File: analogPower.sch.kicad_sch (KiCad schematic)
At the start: 27 parts, among them J1 6120XX21621_61201021621, Q1 MMBT3904, Q2 MMBT3904, U10 TL072, U2 REF02CS, U3 TL072, U8 TL072

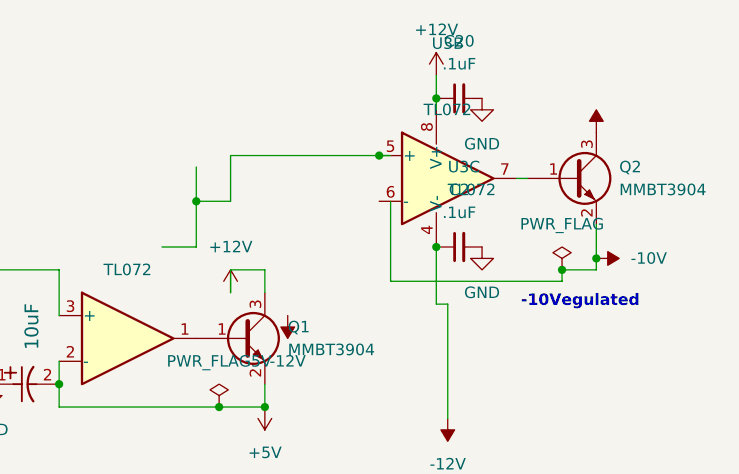
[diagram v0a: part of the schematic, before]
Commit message: added power schematic
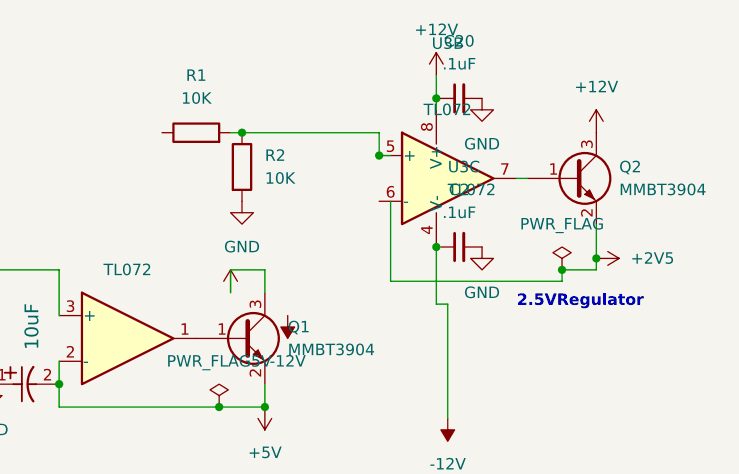
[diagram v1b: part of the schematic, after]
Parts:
- added R1: 10K, Resistor_SMD:R_0603_1608Metric_Pad0.98x0.95mm_HandSolder, symbol Device:R
- added R2: 10K, symbol Device:R
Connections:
- net +12V: now also Q2.3 (C)
- net -12V: no longer Q2.3 (C)
- net GND: now also R2.2
- net at U3.5 (+): now also R1.2, R2.1
- net -10V renamed +2V5
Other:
- note added: "2.5VRegulator"
- note removed: "-10Vegulated"

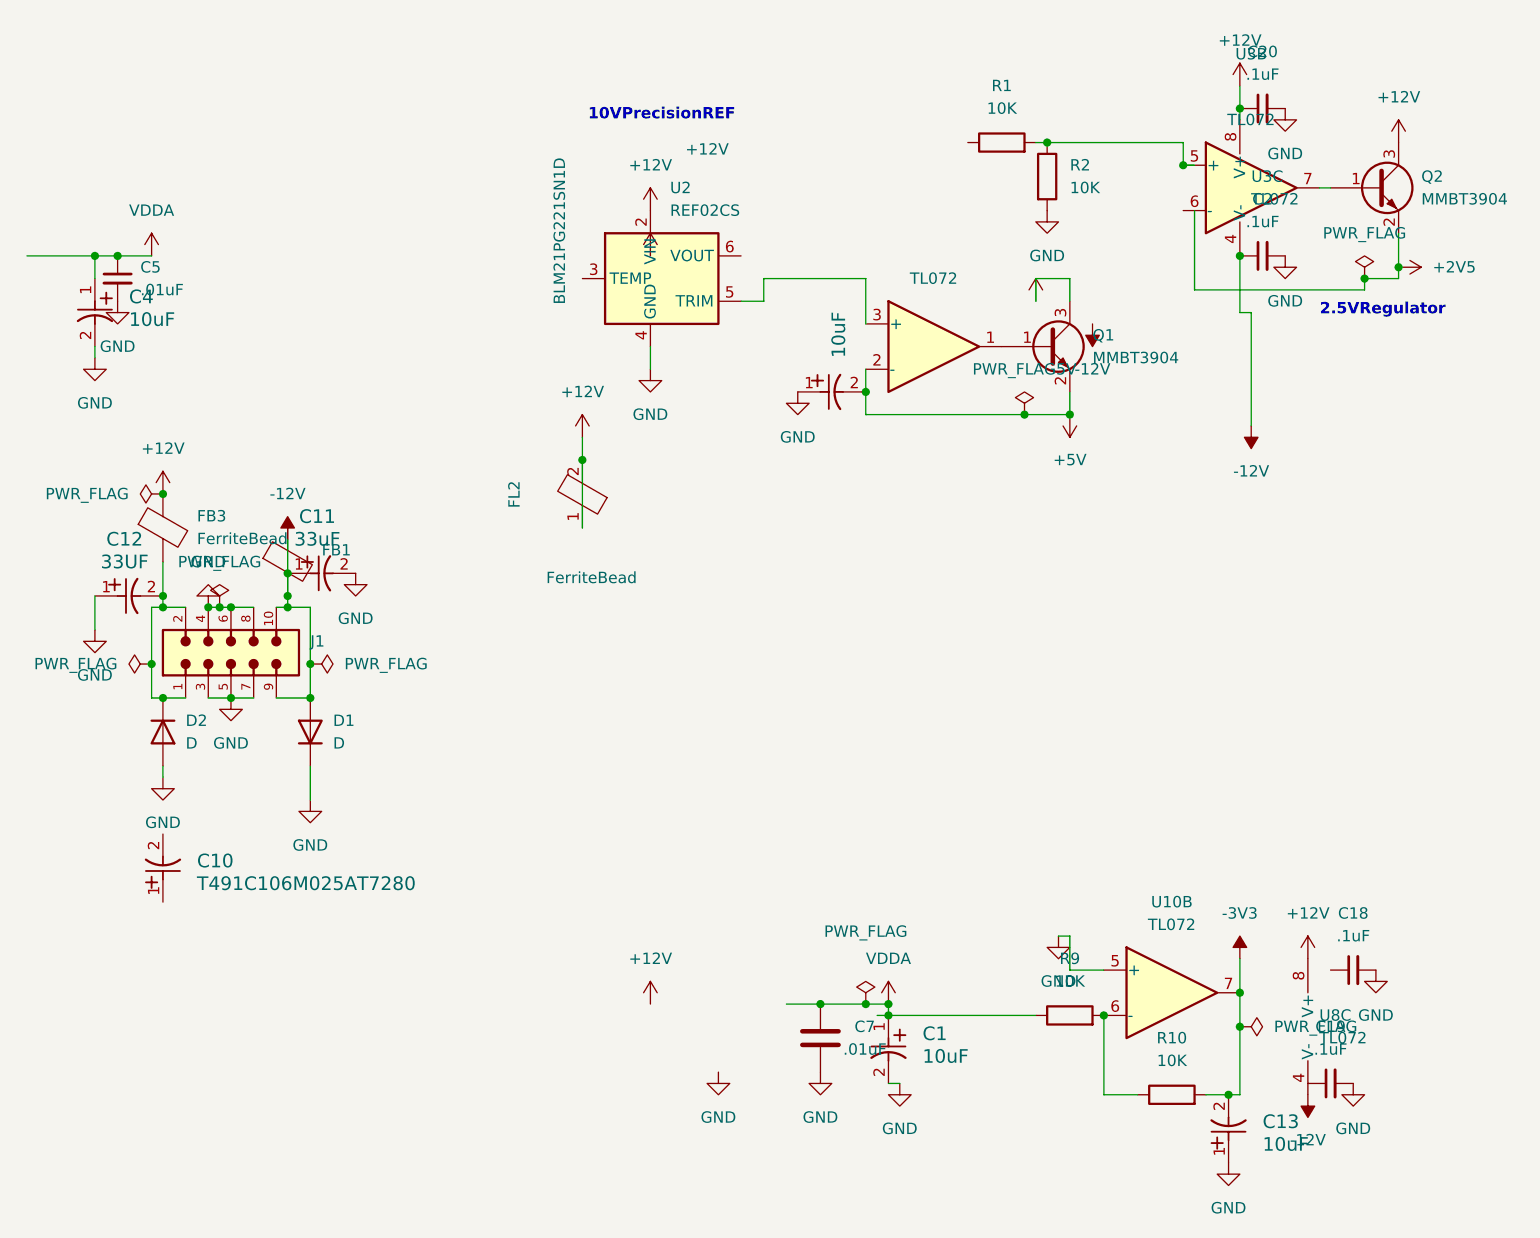
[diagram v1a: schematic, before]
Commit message: AddedFineTune+/-1V
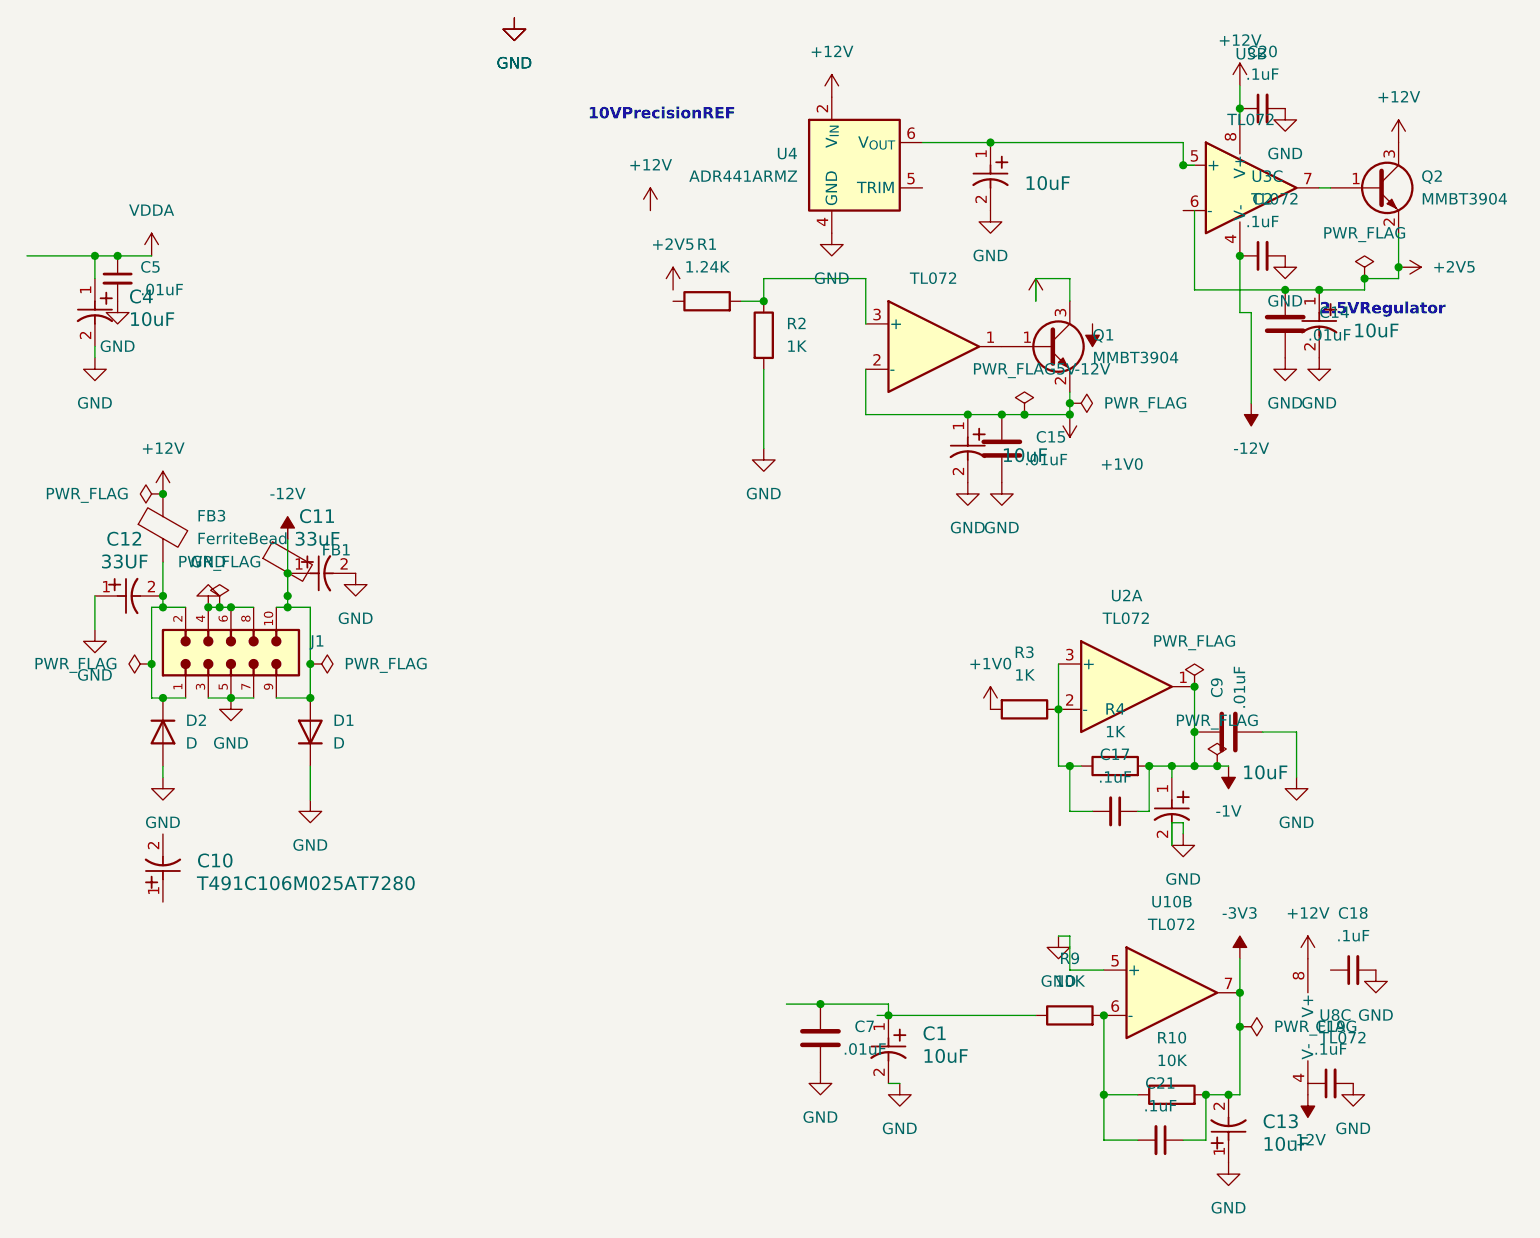
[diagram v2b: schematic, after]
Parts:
- removed C17: 10uF, customfootprints:10uFtantcap, symbol esp32lib:T491C106M025AT7280
- removed FL2: BLM21PG221SN1D, customfootprints:bead, symbol esp32lib:bead
- removed U2: REF02CS, Package_SO:SOIC-8_3.9x4.9mm_P1.27mm, symbol Reference_Voltage:REF02CS
- added C14, C15, C9: .01uF, symbol Device:C
- added C16, C3, C6, C8: 10uF, customfootprints:10uFtantcap, symbol esp32lib:T491C106M025AT7280
- added C17, C21: .1uF, symbol Device:C_Small
- added R3, R4: 1K, symbol Device:R
- added U2: TL072, symbol Amplifier_Operational:TL072
- added U4: ADR441ARMZ, Package_SO:MSOP-8_3x3mm_P0.65mm, symbol Reference_Voltage:ADR441ARMZ
- R1: value 10K -> 1.24K; footprint Resistor_SMD:R_0603_1608Metric_Pad0.98x0.95mm_HandSolder -> (none)
- R2: value 10K -> 1K
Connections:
- net +12V: now also U4.2 (V_{IN})
- net +2V5: now also C14.1, C16.1
- net -3V3: now also C21.1
- net GND: now also C14.2, C15.2, C16.2, C3.2, C6.2, C8.2, C9.2, U4.4 (GND)
- net VDDA: no longer C1.1, C7.1, R9.1
- net at R10.1, R9.2, U10.6 (-): now also C21.2
- net at R1.2, R2.1: now also U3.3 (+); no longer U3.5 (+)
- net +5V renamed +1V0
- net +1V0: now also C15.1, C3.1, R3.2
- new net: C1.1, C7.1, R9.1
- new net: C6.1, U3.5 (+), U4.6 (V_{OUT})
- new net: C17.2, R3.1, R4.1, U2.2 (-), U2.3 (+)
- new net -1V: C17.1, C8.1, C9.1, R4.2, U2.1

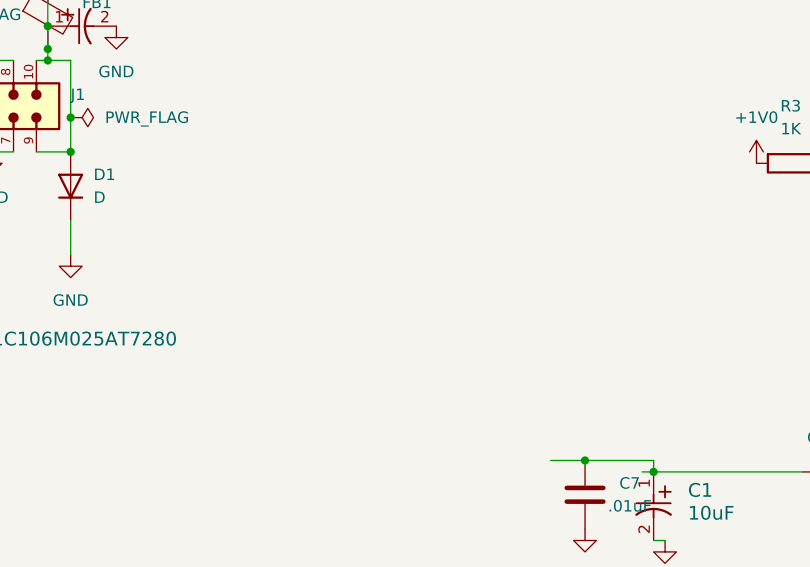
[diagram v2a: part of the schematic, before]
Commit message: added summing opamp
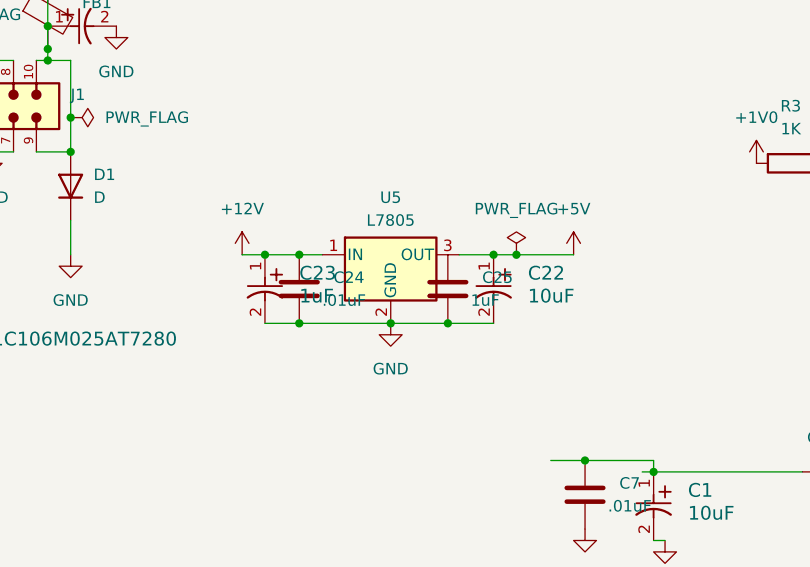
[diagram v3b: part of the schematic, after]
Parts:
- added C22: 10uF, customfootprints:10uFtantcap, symbol esp32lib:T491C106M025AT7280
- added C23: 1uF, customfootprints:10uFtantcap, symbol esp32lib:T491C106M025AT7280
- added C24: .01uF, symbol Device:C
- added C25: 1uF, symbol Device:C
- added U5: L7805, symbol Regulator_Linear:L7805
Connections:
- net +12V: now also C23.1, C24.1, U5.1 (IN)
- net GND: now also C22.2, C23.2, C24.2, C25.2, U5.2 (GND)
- new net +5V: C22.1, U5.3 (OUT)
